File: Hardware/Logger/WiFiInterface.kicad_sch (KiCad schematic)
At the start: 19 parts, among them J10 Conn_01x08_Female, J8 Conn_01x06_Female, J9 Conn_01x08_Female, Q1 FDV304P, Q2 FDV304P, U1 ESP-12E

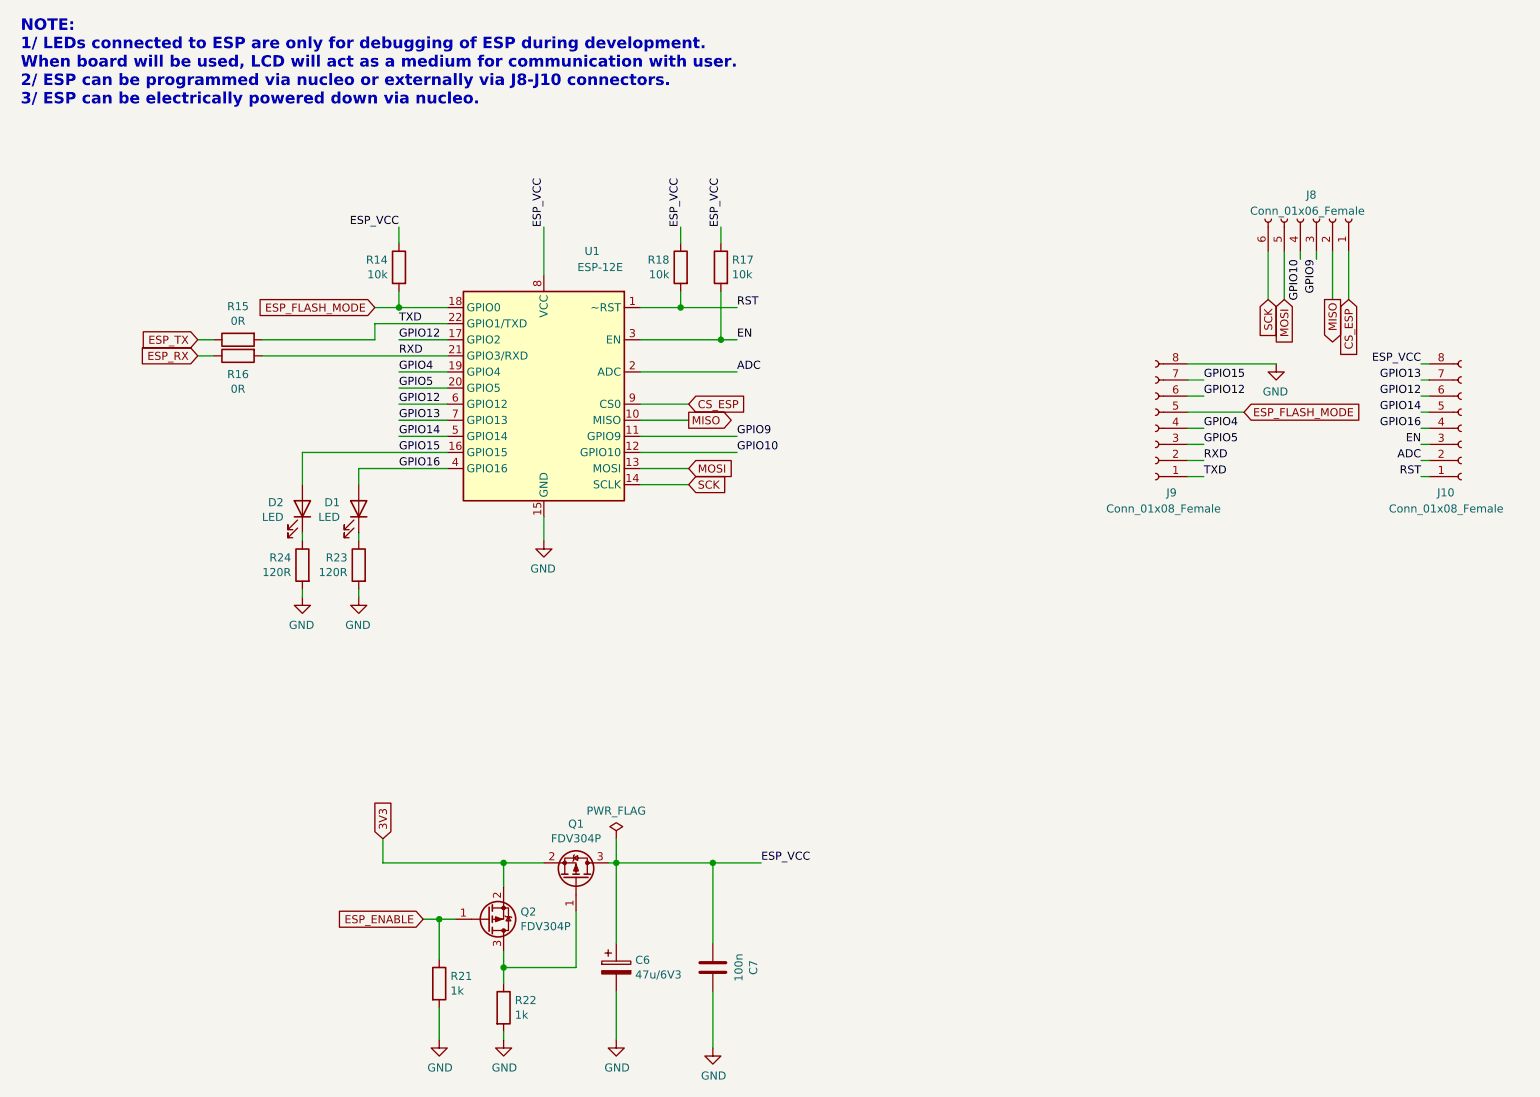
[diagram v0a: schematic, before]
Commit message: PoC of esp32 support (setting esp32 to flashing mode))
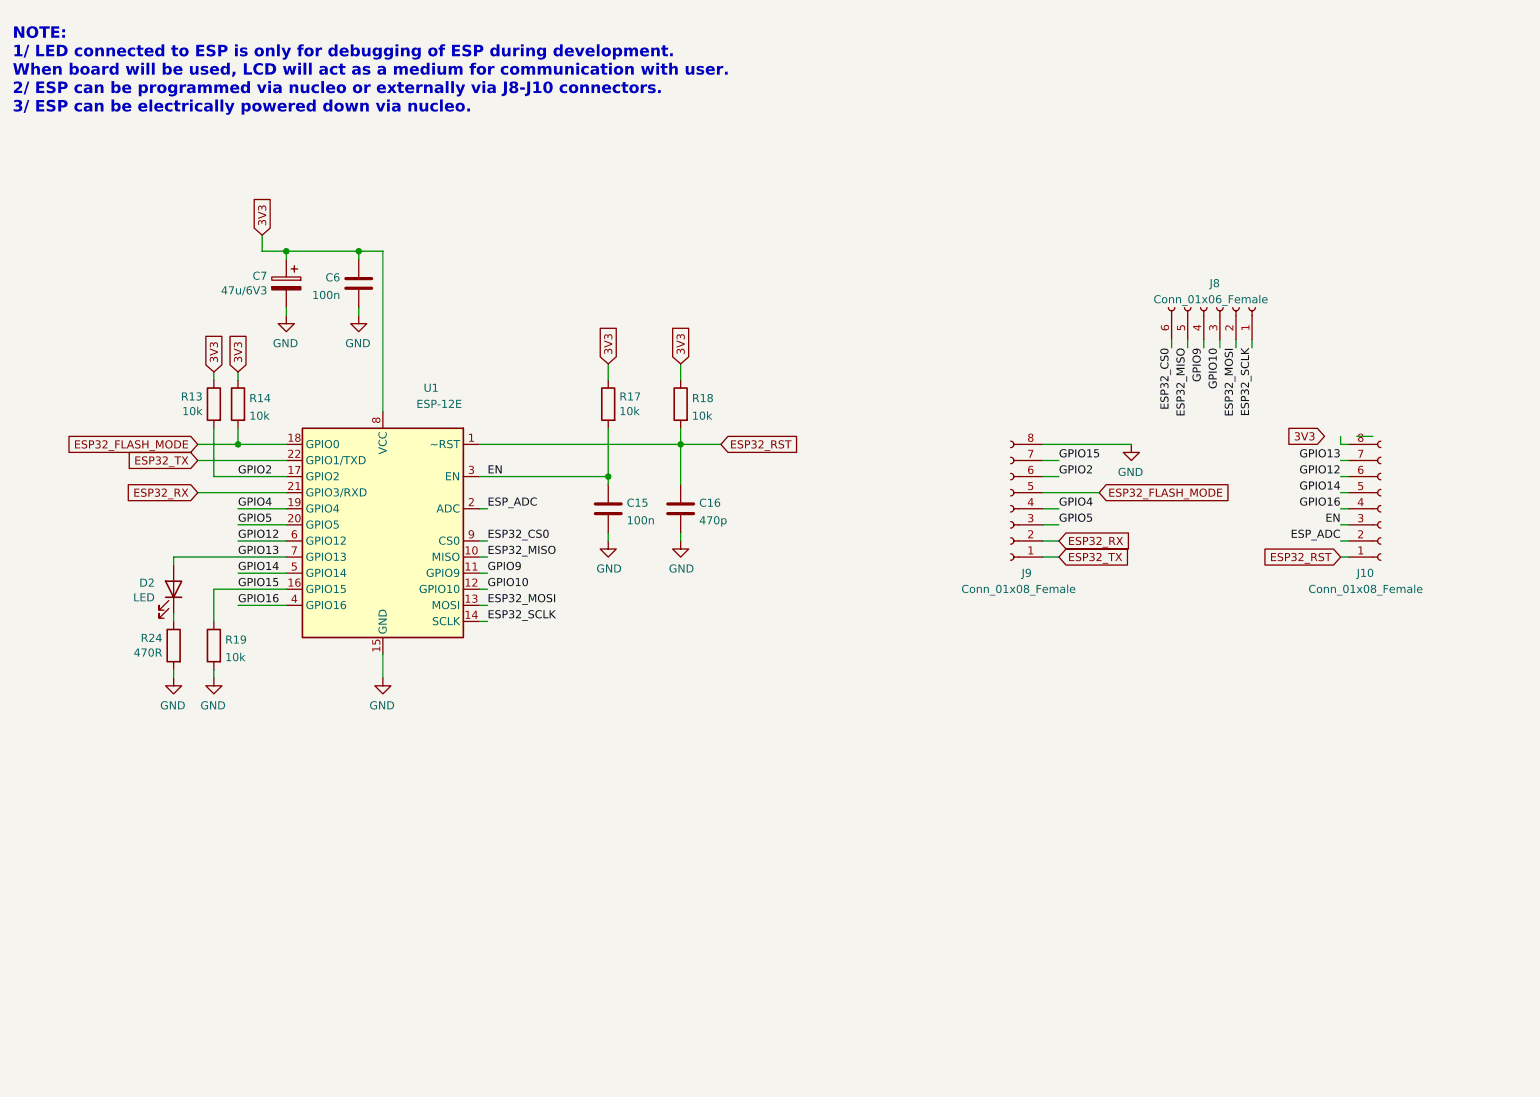
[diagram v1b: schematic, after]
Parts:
- removed C6: 47u/6V3, Capacitor_Tantalum_SMD:CP_EIA-3528-21_Kemet-B, symbol Device:CP
- removed C7: 100n, Capacitor_SMD:C_0805_2012Metric, symbol Device:C
- removed D1: LED, LED_SMD:LED_0402_1005Metric, symbol Device:LED
- removed Q1, Q2: FDV304P, Package_TO_SOT_SMD:SOT-23, symbol Device:Q_PMOS_GSD
- removed R15, R16: 0R, Resistor_SMD:R_0805_2012Metric, symbol Device:R
- removed R21, R22: 1k, Resistor_SMD:R_0805_2012Metric, symbol Device:R
- removed R23: 120R, Resistor_SMD:R_0805_2012Metric, symbol Device:R
- added C15, C6: 100n, Capacitor_SMD:C_0805_2012Metric, symbol Device:C
- added C16: 470p, Capacitor_SMD:C_0805_2012Metric, symbol Device:C
- added C7: 47u/6V3, Capacitor_Tantalum_SMD:CP_EIA-3528-21_Kemet-B, symbol Device:CP
- added R13, R19: 10k, Resistor_SMD:R_0805_2012Metric, symbol Device:R
- R24: value 120R -> 470R
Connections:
- net 3V3: now also R14.1, R17.1, R18.1, U1.8 (VCC), C6.1, C7.1, R13.1
- net EN: now also C15.1
- net GND: now also C15.2, C16.2, C6.2, C7.2, R19.2
- net GPIO10: now also J8.3 (Pin_3); no longer J8.4 (Pin_4)
- net GPIO12: no longer J9.6 (Pin_6), U1.17 (GPIO2)
- net GPIO13: now also D2.2 (A)
- net GPIO15: now also R19.1; no longer D2.2 (A)
- net GPIO9: now also J8.4 (Pin_4); no longer J8.3 (Pin_3)
- net ADC renamed ESP_ADC
- net CS_ESP renamed ESP32_CS0
- net ESP32_CS0: now also J8.6 (Pin_6); no longer J8.1 (Pin_1)
- net ESP_FLASH_MODE renamed ESP32_FLASH_MODE
- removed net ESP_VCC: J10.8 (Pin_8), R14.1, R17.1, R18.1, U1.8 (VCC)
- net MISO renamed ESP32_MISO
- net ESP32_MISO: now also J8.5 (Pin_5); no longer J8.2 (Pin_2)
- net MOSI renamed ESP32_MOSI
- net ESP32_MOSI: now also J8.2 (Pin_2); no longer J8.5 (Pin_5)
- net RST renamed ESP32_RST
- net ESP32_RST: now also C16.1
- net RXD renamed ESP32_RX
- net SCK renamed ESP32_SCLK
- net ESP32_SCLK: now also J8.1 (Pin_1); no longer J8.6 (Pin_6)
- net TXD renamed ESP32_TX
- new net GPIO2: J9.6 (Pin_6), R13.2, U1.17 (GPIO2)
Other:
- note added: "NOTE: 1/ LED connected to ESP is only for debugging of ESP during development. When board will be used, LCD will act as a medium for communication with user. 2/ ESP can be programmed via nucleo or externally via J8-J10 connectors. 3/ ESP can be electrically powered down via nucleo."
- note removed: "NOTE: 1/ LEDs connected to ESP are only for debugging of ESP during development. When board will be used, LCD will act as a medium for communication with user. 2/ ESP can be programmed via nucleo or externally via J8-J10 connectors. 3/ ESP can be electrically powered down via nucleo."
- moved on the sheet: D2, J10, J8, J9, R14, R17, R18, R24, U1

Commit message: apply actual gpio connections to stm32 board, changed photoresistor to phototransistor
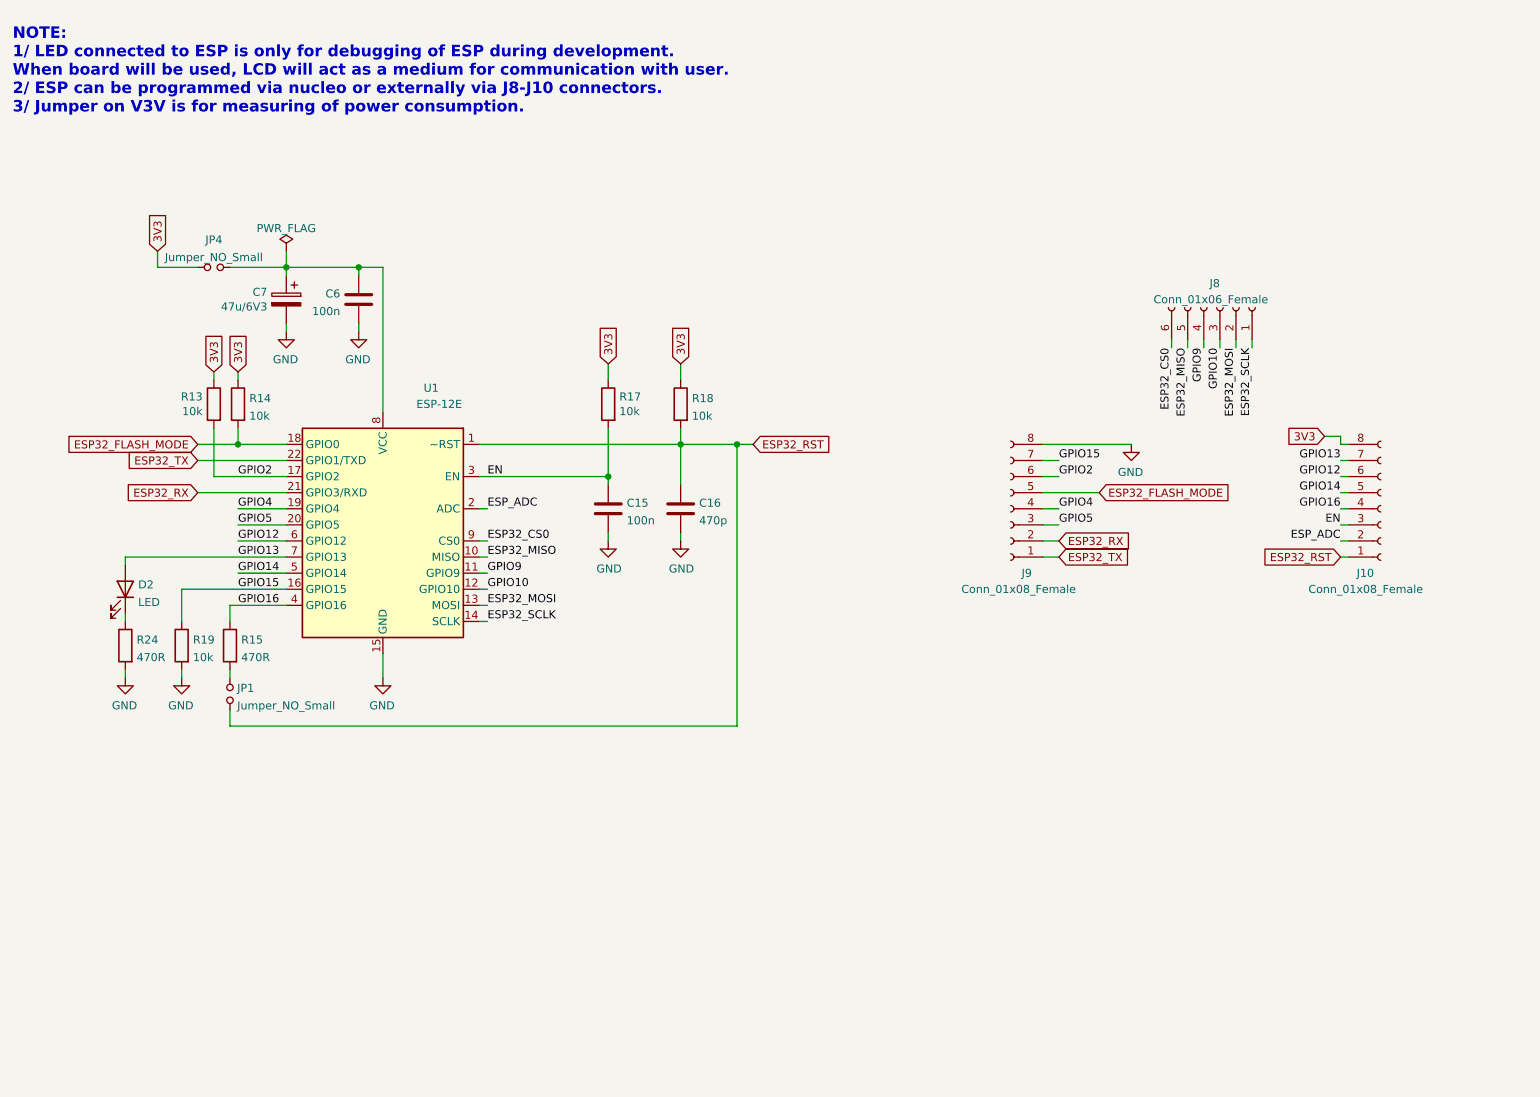
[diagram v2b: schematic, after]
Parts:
- added JP1, JP4: Jumper_NO_Small, symbol Device:Jumper_NO_Small
- added R15: 470R, Resistor_SMD:R_0805_2012Metric, symbol Device:R
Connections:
- net 3V3: now also J10.8 (Pin_8), JP4.1; no longer C6.1, C7.1, U1.8 (VCC)
- net ESP32_RST: now also JP1.1
- net GPIO16: now also R15.1
- new net: C6.1, C7.1, JP4.2, U1.8 (VCC)
- new net: JP1.2, R15.2
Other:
- note added: "NOTE: 1/ LED connected to ESP is only for debugging of ESP during development. When board will be used, LCD will act as a medium for communication with user. 2/ ESP can be programmed via nucleo or externally via J8-J10 connectors. 3/ Jumper on V3V is for measuring of power consumption."
- note removed: "NOTE: 1/ LED connected to ESP is only for debugging of ESP during development. When board will be used, LCD will act as a medium for communication with user. 2/ ESP can be programmed via nucleo or externally via J8-J10 connectors. 3/ ESP can be electrically powered down via nucleo."
- moved on the sheet: C6, C7, D2, R19, R24

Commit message: draft of rev 3.0, cleanup of repo from not fully open source libs
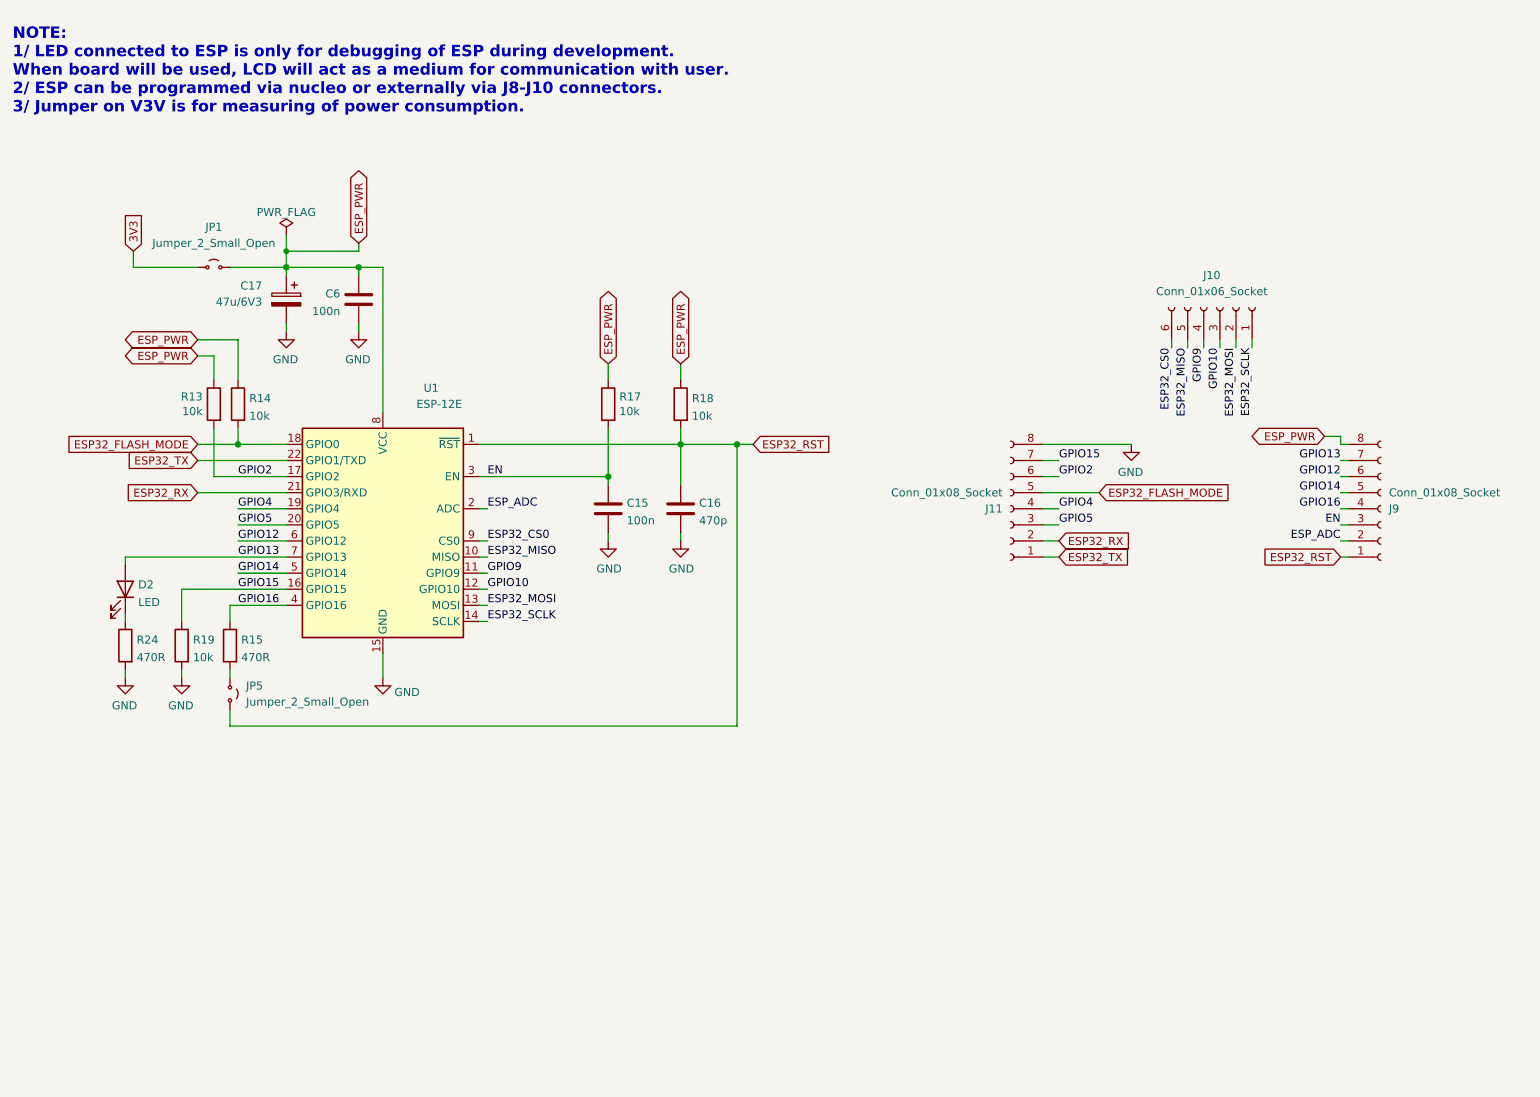
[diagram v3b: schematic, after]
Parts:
- removed C7: 47u/6V3, Capacitor_Tantalum_SMD:CP_EIA-3528-21_Kemet-B, symbol Device:CP
- removed J10, J9: Conn_01x08_Female, Connector_PinSocket_2.54mm:PinSocket_1x08_P2.54mm_Vertical, symbol Connector:Conn_01x08_Female
- removed J8: Conn_01x06_Female, Connector_PinSocket_2.54mm:PinSocket_1x06_P2.54mm_Vertical, symbol Connector:Conn_01x06_Female
- removed JP1, JP4: Jumper_NO_Small, symbol Device:Jumper_NO_Small
- added C17: 47u/6V3, Capacitor_Tantalum_SMD:CP_EIA-3528-21_Kemet-B, symbol Device:C_Polarized
- added J10: Conn_01x06_Socket, Connector_PinSocket_2.54mm:PinSocket_1x06_P2.54mm_Vertical, symbol Connector:Conn_01x06_Socket
- added J11, J9: Conn_01x08_Socket, Connector_PinSocket_2.54mm:PinSocket_1x08_P2.54mm_Vertical, symbol Connector:Conn_01x08_Socket
- added JP1, JP5: Jumper_2_Small_Open, Jumper:SolderJumper-2_P1.3mm_Open_TrianglePad1.0x1.5mm, symbol Jumper:Jumper_2_Small_Open
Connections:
- net 3V3: now also JP1.1 (A); no longer R13.1, R14.1, R17.1, R18.1
- net EN: now also J9.3 (Pin_3)
- net ESP32_CS0: now also J10.6 (Pin_6)
- net ESP32_FLASH_MODE: now also J11.5 (Pin_5)
- net ESP32_MISO: now also J10.5 (Pin_5)
- net ESP32_MOSI: now also J10.2 (Pin_2)
- net ESP32_RST: now also J9.1 (Pin_1), JP5.2 (B)
- net ESP32_RX: now also J11.2 (Pin_2)
- net ESP32_SCLK: now also J10.1 (Pin_1)
- net ESP32_TX: now also J11.1 (Pin_1)
- net ESP_ADC: now also J9.2 (Pin_2)
- net GND: now also C17.2, J11.8 (Pin_8)
- net GPIO10: now also J10.3 (Pin_3)
- net GPIO12: now also J9.6 (Pin_6)
- net GPIO13: now also J9.7 (Pin_7)
- net GPIO14: now also J9.5 (Pin_5)
- net GPIO15: now also J11.7 (Pin_7)
- net GPIO16: now also J9.4 (Pin_4)
- net GPIO2: now also J11.6 (Pin_6)
- net GPIO4: now also J11.4 (Pin_4)
- net GPIO5: now also J11.3 (Pin_3)
- net GPIO9: now also J10.4 (Pin_4)
- net ESP_PWR: now reaches C6.1, U1.8 (VCC)
- net ESP_PWR: now also R13.1, R14.1, R17.1, R18.1, C17.1, J9.8 (Pin_8), JP1.2 (B)
- net at R15.2: now also JP5.1 (A)
